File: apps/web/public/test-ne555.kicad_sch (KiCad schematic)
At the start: 9 parts, among them J1 PWR_5V, U1 NE555P

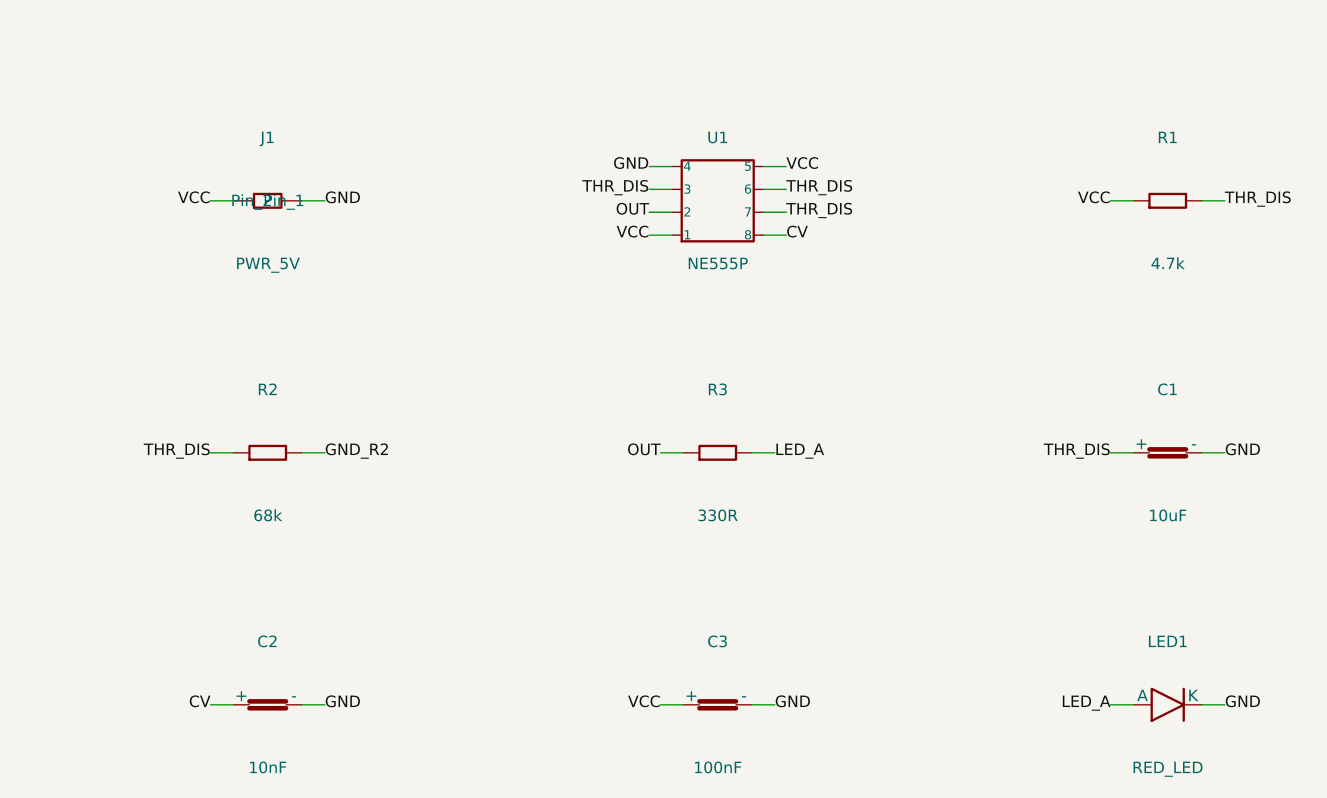
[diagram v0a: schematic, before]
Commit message: feat(kicad): Timer:NE555P named pins + compact paper for better zoom
- Add Timer:NE555P inline symbol with proper named pins:
  GND(1) TRIG(2) OUT(3) RST(4) CTRL(5) THR(6) DIS(7) VCC(8)
- _simple_lib_id: detect NE555/LM555/NA555/TLC555/ICM7555 → Timer:NE555P
- _pin_offset: Timer:NE555P reuses DIP-8 _IC_PIN_OFFSETS geometry
- Reduce paper margins 20→8mm, col_step 50→45, row_step 28→25
  LM7805 paper: 165x88 → 128x59mm (-40%) = composants 40% plus grands
  au zoom-to-fit KiCanvas
- Regenerate 3 fixtures (lm7805/ne555/esp32)
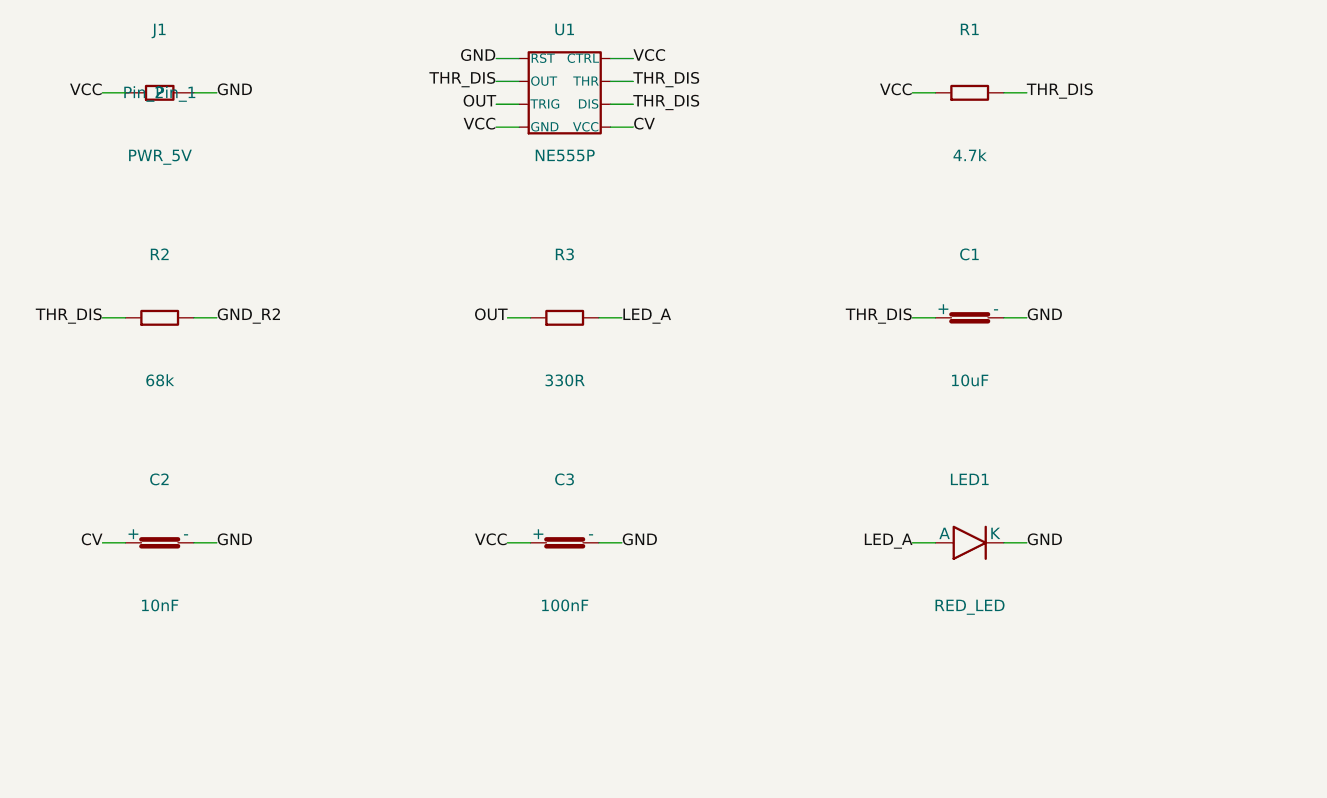
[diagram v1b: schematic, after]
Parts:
- removed U1: NE555P, Package_DIP:DIP-8_W7.62mm, symbol Device:IC
- added U1: NE555P, Package_DIP:DIP-8_W7.62mm, symbol Timer:NE555P
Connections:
- net CV: now also U1.8 (VCC)
- net GND: now also U1.4 (RST)
- net OUT: now also U1.2 (TRIG)
- net THR_DIS: now also U1.3 (OUT), U1.6 (THR), U1.7 (DIS)
- net VCC: now also U1.1 (GND), U1.5 (CTRL)
